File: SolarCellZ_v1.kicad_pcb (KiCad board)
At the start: 6 copper layers, 48.4 x 48.4 mm, 62 parts, among them IC1 TSL2561, J1 XF2M-1015-1A, Q1 IRLML2803, U1 NDS8434, U2 Value

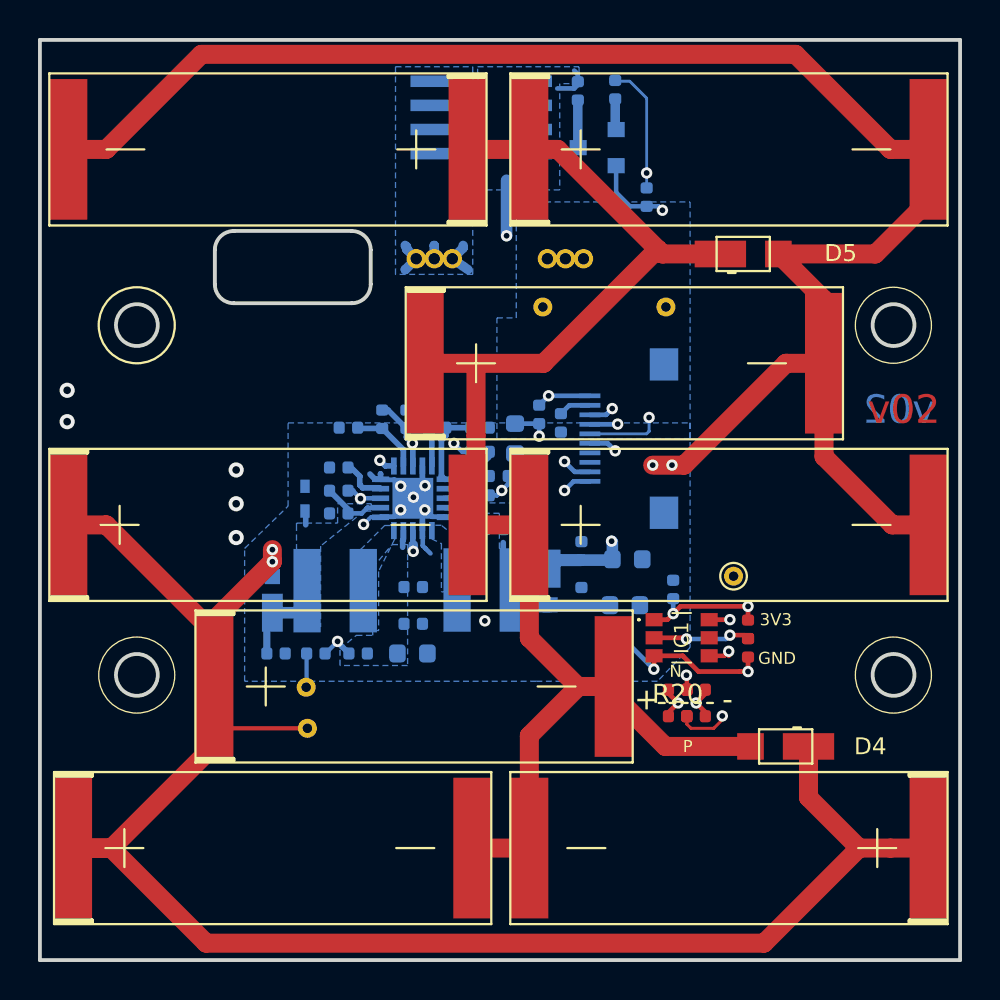
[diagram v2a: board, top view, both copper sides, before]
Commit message: added fiducials, regenerated 3d model and gerbers
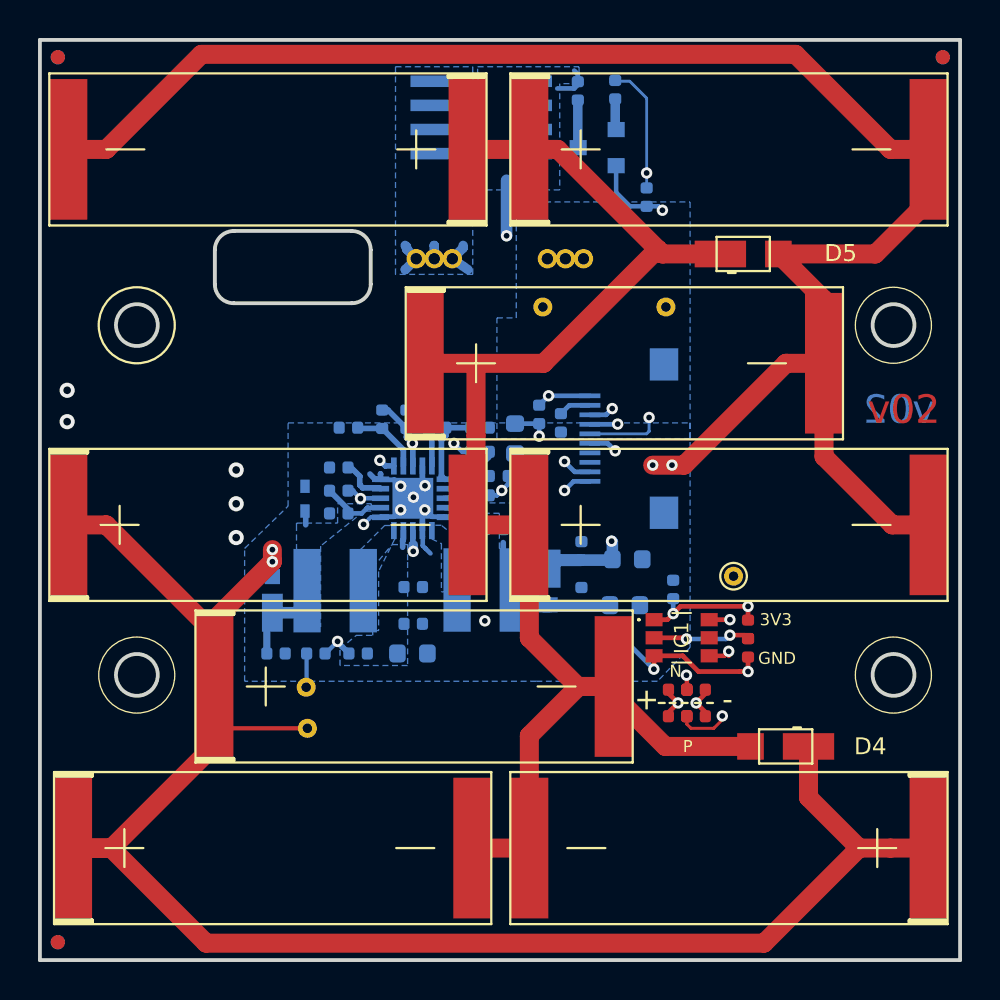
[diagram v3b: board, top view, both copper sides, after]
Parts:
- added REF**: Fiducial_0.75mm_Mask1.5mm, Fiducial:Fiducial_0.75mm_Mask1.5mm, B.Cu at (91.0, 87.5)
- added REF**: Fiducial_0.75mm_Mask1.5mm, Fiducial:Fiducial_0.75mm_Mask1.5mm, B.Cu at (91.0, 40.9)
- added REF**: Fiducial_0.75mm_Mask1.5mm, Fiducial:Fiducial_0.75mm_Mask1.5mm, B.Cu at (137.5, 40.9)
- added REF**: Fiducial_0.75mm_Mask1.5mm, Fiducial:Fiducial_0.75mm_Mask1.5mm, F.Cu at (137.5, 40.9)
- added REF**: Fiducial_0.75mm_Mask1.5mm, Fiducial:Fiducial_0.75mm_Mask1.5mm, F.Cu at (91.0, 40.9)
- added REF**: Fiducial_0.75mm_Mask1.5mm, Fiducial:Fiducial_0.75mm_Mask1.5mm, F.Cu at (91.0, 87.5)
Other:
- board text removed: "v00"
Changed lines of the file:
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@@
   (general
     (thickness 1.6)
-    (drawings 60)
+    (drawings 58)
     (tracks 3130)
     (zones 0)
-    (modules 62)
+    (modules 68)
     (nets 32)
   )
@@
   (layers
     (0 Top signal)
-    (1 In1.Cu signal)
-    (2 In2.Cu signal)
-    (3 In3.Cu signal)
+    (1 In1.Cu signal hide)
+    (2 In2.Cu signal hide)
+    (3 In3.Cu signal hide)
     (4 In4.Cu signal hide)
     (31 Bottom signal)
@@
     (34 B.Paste user hide)
     (35 F.Paste user hide)
-    (36 B.SilkS user hide)
+    (36 B.SilkS user)
     (37 F.SilkS user)
     (38 B.Mask user)
-    (39 F.Mask user hide)
+    (39 F.Mask user)
     (40 Dwgs.User user hide)
     (41 Cmts.User user hide)
@@
     (add_net VSOLAR)
   )
+  (module Fiducial:Fiducial_0.75mm_Mask1.5mm (layer Bottom)
+    (at 90.95 87.45)
+    (descr "Circular Fiducial, 0.75mm bare copper, 1.5mm soldermask opening (Level B)")
+    (tags fiducial)
+    (attr smd)
+    (fp_text reference REF** (at 0 2) (layer B.SilkS) hide
+      (effects (font (size 1 1) (thickness 0.15)) (justify mirror))
+    )
+    (fp_text value Fiducial_0.75mm_Mask1.5mm (at 0 -2) (layer B.Fab)
+      (effects (font (size 1 1) (thickness 0.15)) (justify mirror))
+    )
+    (fp_circle (center 0 0) (end 0.75 0) (layer B.Fab) (width 0.1))
+    (fp_text user %R (at 0 0) (layer B.Fab)
+      (effects (font (size 0.3 0.3) (thickness 0.05)) (justify mirror))
+    )
+    (fp_circle (center 0 0) (end 1 0) (layer B.CrtYd) (width 0.05))
+    (pad "" smd circle (at 0 0) (size 0.75 0.75) (layers Bottom B.Mask)
+      (solder_mask_margin 0.375) (clearance 0.375))
+  )
+  (module Fiducial:Fiducial_0.75mm_Mask1.5mm (layer Bottom)
+    (at 90.95 40.9)
+    (descr "Circular Fiducial, 0.75mm bare copper, 1.5mm soldermask opening (Level B)")
+    (tags fiducial)
+    (attr smd)
+    (fp_text reference REF** (at 0 2) (layer B.SilkS) hide
+      (effects (font (size 1 1) (thickness 0.15)) (justify mirror))
+    )
+    (fp_text value Fiducial_0.75mm_Mask1.5mm (at 0 -2) (layer B.Fab)
+      (effects (font (size 1 1) (thickness 0.15)) (justify mirror))
+    )
+    (fp_circle (center 0 0) (end 1 0) (layer B.CrtYd) (width 0.05))
+    (fp_text user %R (at 0 0) (layer B.Fab)
+      (effects (font (size 0.3 0.3) (thickness 0.05)) (justify mirror))
+    )
+    (fp_circle (center 0 0) (end 0.75 0) (layer B.Fab) (width 0.1))
+    (pad "" smd circle (at 0 0) (size 0.75 0.75) (layers Bottom B.Mask)
+      (solder_mask_margin 0.375) (clearance 0.375))
+  )
+  (module Fiducial:Fiducial_0.75mm_Mask1.5mm (layer Bottom)
+    (at 137.5 40.9)
+    (descr "Circular Fiducial, 0.75mm bare copper, 1.5mm soldermask opening (Level B)")
+    (tags fiducial)
+    (attr smd)
+    (fp_text reference REF** (at 0 2) (layer B.SilkS) hide
+      (effects (font (size 1 1) (thickness 0.15)) (justify mirror))
+    )
+    (fp_text value Fiducial_0.75mm_Mask1.5mm (at 0 -2) (layer B.Fab)
+      (effects (font (size 1 1) (thickness 0.15)) (justify mirror))
+    )
+    (fp_circle (center 0 0) (end 0.75 0) (layer B.Fab) (width 0.1))
+    (fp_text user %R (at 0 0) (layer B.Fab)
+      (effects (font (size 0.3 0.3) (thickness 0.05)) (justify mirror))
+    )
+    (fp_circle (center 0 0) (end 1 0) (layer B.CrtYd) (width 0.05))
+    (pad "" smd circle (at 0 0) (size 0.75 0.75) (layers Bottom B.Mask)
+      (solder_mask_margin 0.375) (clearance 0.375))
+  )
+  (module Fiducial:Fiducial_0.75mm_Mask1.5mm (layer Top)
+    (at 137.5 40.9)
+    (descr "Circular Fiducial, 0.75mm bare copper, 1.5mm soldermask opening (Level B)")
+    (tags fiducial)
+    (attr smd)
+    (fp_text reference REF** (at 0 -2) (layer F.SilkS) hide
+      (effects (font (size 1 1) (thickness 0.15)))
+    )
+    (fp_text value Fiducial_0.75mm_Mask1.5mm (at 0 2) (layer F.Fab)
+      (effects (font (size 1 1) (thickness 0.15)))
+    )
+    (fp_circle (center 0 0) (end 1 0) (layer F.CrtYd) (width 0.05))
+    (fp_text user %R (at 0 0) (layer F.Fab)
+      (effects (font (size 0.3 0.3) (thickness 0.05)))
+    )
+    (fp_circle (center 0 0) (end 0.75 0) (layer F.Fab) (width 0.1))
+    (pad "" smd circle (at 0 0) (size 0.75 0.75) (layers Top F.Mask)
+      (solder_mask_margin 0.375) (clearance 0.375))
+  )
+  (module Fiducial:Fiducial_0.75mm_Mask1.5mm (layer Top)
+    (at 90.95 40.9)
+    (descr "Circular Fiducial, 0.75mm bare copper, 1.5mm soldermask opening (Level B)")
+    (tags fiducial)
+    (attr smd)
+    (fp_text reference REF** (at 0 -2) (layer F.SilkS) hide
+      (effects (font (size 1 1) (thickness 0.15)))
+    )
+    (fp_text value Fiducial_0.75mm_Mask1.5mm (at 0 2) (layer F.Fab)
+      (effects (font (size 1 1) (thickness 0.15)))
+    )
+    (fp_circle (center 0 0) (end 0.75 0) (layer F.Fab) (width 0.1))
+    (fp_text user %R (at 0 0) (layer F.Fab)
+      (effects (font (size 0.3 0.3) (thickness 0.05)))
+    )
+    (fp_circle (center 0 0) (end 1 0) (layer F.CrtYd) (width 0.05))
+    (pad "" smd circle (at 0 0) (size 0.75 0.75) (layers Top F.Mask)
+      (solder_mask_margin 0.375) (clearance 0.375))
+  )
   (module custom-footprints:KXOB25-05X3F (layer Top)
     (at 115.75 45.75)
@@
     (tags resistor)
     (attr smd)
-    (fp_text reference R19 (at 1.778 0.0635 270) (layer B.SilkS)
+    (fp_text reference R19 (at -0.028 3.4495 270) (layer B.SilkS)
       (effects (font (size 0.889 0.889) (thickness 0.127)) (justify mirror))
     )
@@
     (tags resistor)
     (attr smd)
-    (fp_text reference R4 (at 1.7145 0.127 270) (layer B.SilkS)
+    (fp_text reference R4 (at 0.3085 2.731 270) (layer B.SilkS)
       (effects (font (size 0.889 0.889) (thickness 0.127)) (justify mirror))
     )
@@
     (tags resistor)
     (attr smd)
-    (fp_text reference R20 (at 0 -1.17) (layer F.SilkS)
+    (fp_text reference R20 (at -0.2 1.435) (layer F.SilkS) hide
       (effects (font (size 1 1) (thickness 0.15)))
     )
@@
       (rotate (xyz 0 0 0))
     )
+  )
+  (module Fiducial:Fiducial_0.75mm_Mask1.5mm (layer Top)
+    (at 90.95 87.45)
+    (descr "Circular Fiducial, 0.75mm bare copper, 1.5mm soldermask opening (Level B)")
+    (tags fiducial)
+    (attr smd)
+    (fp_text reference REF** (at 0 -2) (layer F.SilkS) hide
+      (effects (font (size 1 1) (thickness 0.15)))
+    )
+    (fp_text value Fiducial_0.75mm_Mask1.5mm (at 0 2) (layer F.Fab)
+      (effects (font (size 1 1) (thickness 0.15)))
+    )
+    (fp_circle (center 0 0) (end 1 0) (layer F.CrtYd) (width 0.05))
+    (fp_text user %R (at 0 0) (layer F.Fab)
+      (effects (font (size 0.3 0.3) (thickness 0.05)))
+    )
+    (fp_circle (center 0 0) (end 0.75 0) (layer F.Fab) (width 0.1))
+    (pad "" smd circle (at 0 0) (size 0.75 0.75) (layers Top F.Mask)
+      (solder_mask_margin 0.375) (clearance 0.375))
   )
   (gr_text 1 (at 120.45 55.2) (layer B.SilkS)
@@
     (effects (font (size 0.635 0.635) (thickness 0.127)))
   )
-  (gr_text v00 (at 252.7935 145.669) (layer F.Mask)
-    (effects (font (size 1.5 1.5) (thickness 0.3)))
-  )
   (gr_text N (at 123.444 73.152 180) (layer F.SilkS)
     (effects (font (size 0.635 0.635) (thickness 0.127)))
@@
   (gr_circle (center 134.9 55) (end 136.9 55) (layer F.SilkS) (width 0.05))
   (gr_circle (center 95.1 55) (end 97.1 55) (layer F.SilkS) (width 0.12))
-  (gr_text v00 (at 252.5395 145.669) (layer B.Mask)
-    (effects (font (size 1.5 1.5) (thickness 0.3)) (justify mirror))
-  )
   (via (at 126.3 71.3) (size 0.6) (drill 0.3) (layers Top Bottom) (net 1))
   (segment (start 126.342 71.478) (end 126.3015 71.4375) (width 0.24892) (layer Top) (net 1))
